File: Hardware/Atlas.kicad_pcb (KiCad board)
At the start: 2 copper layers, 80.5 x 70 mm, 48 parts, among them J1 DC, U1 MS5611, U2 HTU21D, U3 uSD Card, U4 RFD900, U5 MPU9150, U6 XBEE, U7 VENUS838LPX-L, U8 AOZ1031

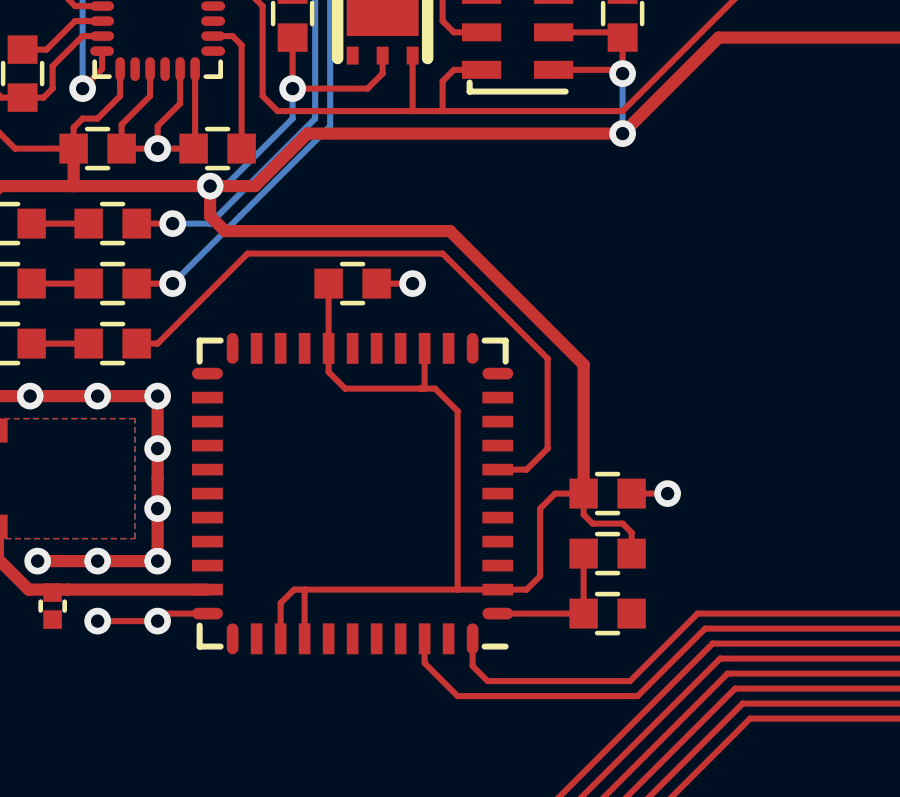
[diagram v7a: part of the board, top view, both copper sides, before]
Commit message: Update GPS to support Flash and ROM versions
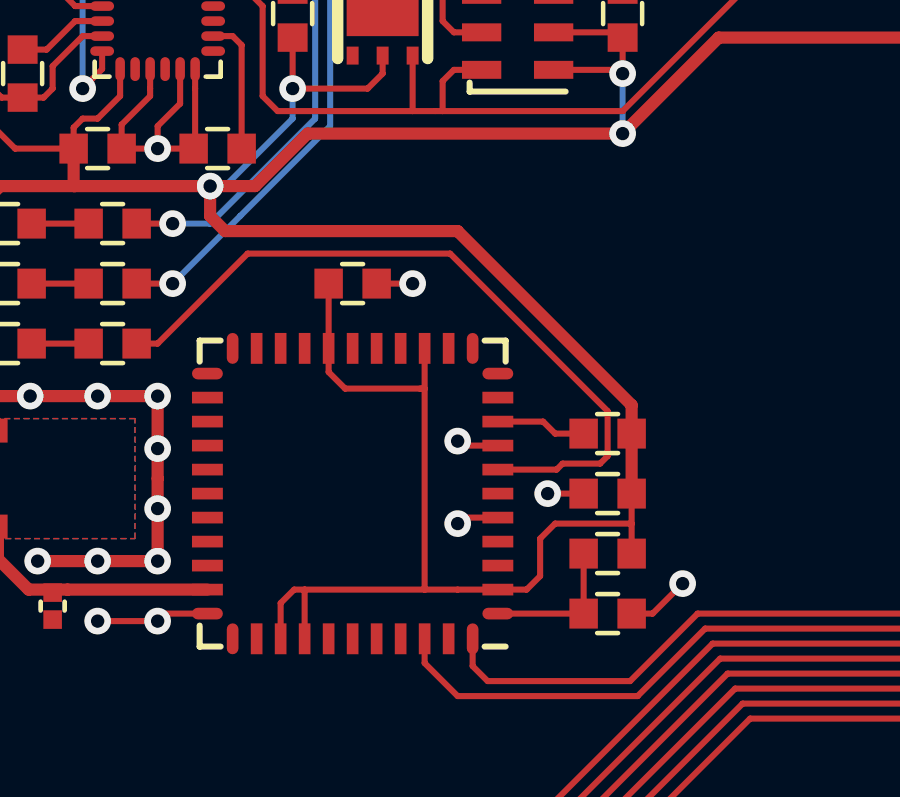
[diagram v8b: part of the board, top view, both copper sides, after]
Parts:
- added R12: 10k, RESC1608-N, F.Cu at (122.5, 93.0)
- U7: value VENUS838LPX-L -> VENUS838FLPX-L
- turned C13 to 180 degrees
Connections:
- U7 pad 9: (no net) -> N-0000025
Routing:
- net GND: track 106.1 -> 111.0 mm, vias 34 -> 37
- net /NAV: track 21.3 -> 24.5 mm
- net N-0000025: track 0.00 -> 3.03 mm
- net +3.3V: track 395.7 -> 395.0 mm
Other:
- board text added: "Atlas v1.1"
- board text removed: "Atlas v1.0"
